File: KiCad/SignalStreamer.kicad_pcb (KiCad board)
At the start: 2 copper layers, 100.3 x 59.1 mm, 48 parts, among them J105 Conn_01x02, T101 Coupled_Inductors_2

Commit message: Ver X1.0
Copied latest changes from backup project
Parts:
- added REF**: MountingHole_2.5mm, MountingHole:MountingHole_2.5mm, F.Cu at (75.2, 86.3)
- added REF**: MountingHole_2.5mm, MountingHole:MountingHole_2.5mm, F.Cu at (96.1, 71.0)
- added REF**: MountingHole_2.5mm, MountingHole:MountingHole_2.5mm, F.Cu at (87.6, 75.4)
- added REF**: MountingHole_2.5mm, MountingHole:MountingHole_2.5mm, F.Cu at (69.9, 63.5)
- added REF**: MountingHole_2.5mm, MountingHole:MountingHole_2.5mm, F.Cu at (74.9, 71.6)
- added REF**: MountingHole_2.5mm, MountingHole:MountingHole_2.5mm, F.Cu at (70.3, 94.6)
- T101: footprint Inductor_THT:Core_150A_2_windings_Horiz_TH -> Inductor_THT:Core_T130_2_windings_Horiz_TH
- moved L101 19.5 mm to (119.0, 63.3), turned to -90 degrees
- moved L101 18.6 mm to (120.6, 63.3), turned to -90 degrees
- moved REF** 12.3 mm to (134.4, 75.5)
- moved REF** 11.4 mm to (134.8, 101.7)
- moved L101 10.9 mm to (102.7, 79.5), turned to -90 degrees
- moved L101 10.8 mm to (101.2, 79.5), turned to -90 degrees
- moved ? 8.33 mm to (123.0, 67.2)
- moved REF** 4.90 mm to (126.7, 63.3)
- moved ? 4.00 mm to (103.9, 106.2)
- moved ? 4.00 mm to (103.9, 112.8)
- moved REF** 4.00 mm to (103.9, 99.7)
- moved ? 3.24 mm to (122.7, 108.3)
- moved T101 3.16 mm to (79.6, 78.9)
- moved REF** 2.91 mm to (126.7, 112.7)
- moved C101 2.83 mm to (97.2, 97.5)
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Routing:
- net Net-(J105-Pin_1): track 13.0 -> 34.3 mm
- net Net-(T101-IN+): track 3.23 -> 7.65 mm
- net Net-(T101-OUT1B): track 8.37 -> 5.29 mm
- net Net-(AE101-A): track 24.8 -> 27.3 mm
- net Net-(D101-K): track 13.7 -> 13.0 mm
- net Net-(D101-A): track 74.0 -> 74.5 mm
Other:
- board text added: "*"
- board text added: "Braid"
- board text added: "Coax"
- board text added: "Counterpoise Elements*"
- board text added: "SignalStreamer Ver 1.0 1 Jan 2026"
- board text added: "Tube"
- board text added: "Vertical"

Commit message: Development
Updates
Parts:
- removed the ? at (118.0, 106.2)
- removed the ? at (118.0, 99.7)
- removed the ? at (118.0, 112.8)
- removed the ? at (103.9, 106.2)
- removed the ? at (103.9, 112.8)
- removed the L101 at (101.2, 79.5)
- removed the L101 at (102.7, 79.5)
- removed the L101 at (119.0, 63.3)
- removed the REF** at (103.9, 99.7)
- added REF**: L_Lipstick_Tube_Variable, Inductor_THT:L_Lipstick_Tube_Variable, F.Cu at (101.2, 79.6)
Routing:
- net Net-(J105-Pin_1): track 34.3 -> 36.2 mm

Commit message: Development
PCB Updates
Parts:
- removed the L101 at (120.6, 63.3)
- L101: renamed from REF**; value L_Lipstick_Tube_Variable -> FB-31-4852
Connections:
- L101 pad 1: (no net) -> Net-(T101-OUT1B)
- L101 pad 2: (no net) -> Net-(J105-Pin_1)
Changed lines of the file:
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@@
 			)
 		)
+		(property "Digi-Key Part No." ""
+			(at 0 0 0)
+			(unlocked yes)
+			(layer "F.Fab")
+			(hide yes)
+			(effects
+				(font
+					(size 1 1)
+					(thickness 0.15)
+				)
+			)
+		)
 		(sheetname "/")
 		(sheetfile "SignalStreamer.kicad_sch")
@@
 			(pinfunction "OUT1A")
 			(pintype "passive")
+			(clearance 0.5)
 			(zone_connect 2)
 		)
@@
 			(pinfunction "OUT1B")
 			(pintype "passive")
+			(clearance 0.5)
 			(zone_connect 2)
 		)
@@
 			)
 		)
-		(property "Datasheet" ""
+		(property "Datasheet" "~"
 			(at 0 0 90)
 			(layer "F.Fab")
@@
 			)
 		)
-		(property "Description" "CONN BNC JACK R/A 50 OHM PCB"
+		(property "Description" "Generic connector, single row, 01x02, script generated (kicad-library-utils/schlib/autogen/connector/)"
 			(at 37.8625 216.6875 0)
 			(layer "F.Fab")
@@
 			)
 		)
-		(property "Link" "https://www.digikey.com/en/products/detail/amphenol-rf/31-5431/80179?utm_adgroup=Coaxial%20Connectors%20%28RF%29&utm_source=google&utm_medium=cpc&utm_campaign=Shopping_Product_Connectors%2C%20Interconnects&utm_term=&utm_content=Coaxial%20Connectors%20%28RF%29&gclid=Cj0KCQjw1rqkBhCTARIsAAHz7K07BKQI4hz-lx2UKWOAkhojF887qRyZwSAGP9HUwnWBejkHZJLi92kaAsMsEALw_wcB"
+		(property "Link" ""
 			(at 37.8625 216.6875 0)
 			(layer "F.Fab")
@@
 			)
 		)
-		(property "Manufacturer" "Amphenol RF"
+		(property "Manufacturer" ""
 			(at 37.8625 216.6875 0)
 			(layer "F.Fab")
@@
 			)
 		)
-		(property "Manufacturer PN" "31-5431"
+		(property "Manufacturer PN" ""
 			(at 37.8625 216.6875 0)
 			(layer "F.Fab")
@@
 			)
 		)
+		(property "Sim.Device" ""
+			(at 0 0 270)
+			(unlocked yes)
+			(layer "F.Fab")
+			(hide yes)
+			(effects
+				(font
+					(size 1 1)
+					(thickness 0.15)
+				)
+			)
+		)
+		(property "Sim.Pins" ""
+			(at 0 0 270)
+			(unlocked yes)
+			(layer "F.Fab")
+			(hide yes)
+			(effects
+				(font
+					(size 1 1)
+					(thickness 0.15)
+				)
+			)
+		)
 		(property ki_fp_filters "Connector*:*_1x??_*")
 		(sheetname "/")
 		(sheetfile "SignalStreamer.kicad_sch")
-		(attr through_hole)
+		(attr through_hole exclude_from_bom)
 		(fp_line
 			(start -7.5 2.3)
@@
 	(footprint ""
 		(layer "F.Cu")
-		(at 120.58 63.31 -90)
-		(property "Reference" "L101"
-			(at 0 0 90)
-			(layer "F.SilkS")
-			(hide yes)
-			(effects
-				(font
-					(size 1.27 1.27)
-					(thickness 0.15)
-				)
-			)
-		)
-		(property "Value" "0.4-1.0uH"
-			(at 0 0 90)
-			(layer "F.Fab")
-			(effects
-				(font
-					(size 1.27 1.27)
-					(thickness 0.15)
-				)
-			)
-		)
-		(property "Datasheet" ""
-			(at 0 0 90)
-			(layer "F.Fab")
-			(hide yes)
-			(effects
-				(font
-					(size 1.27 1.27)
-					(thickness 0.15)
-				)
-			)
-		)
-		(property "Description" ""
-			(at 0 0 90)
-			(layer "F.Fab")
-			(hide yes)
-			(effects
-				(font
-					(size 1.27 1.27)
-					(thickness 0.15)
-				)
-			)
-		)
-		(sheetname "/")
-		(sheetfile "SignalStreamer.kicad_sch")
-		(pad "2" thru_hole circle
-			(at 0 0 270)
-			(size 2.6 2.6)
-			(drill 1.1)
-			(layers "*.Cu" "*.Mask")
-			(remove_unused_layers no)
-			(net 15 "Net-(J105-Pin_1)")
-			(pinfunction "2")
-			(pintype "passive")
-			(clearance 0.5)
-			(zone_connect 2)
-		)
-		(embedded_fonts no)
-	)
-	(footprint ""
-		(layer "F.Cu")
 		(at 122.97 67.19)
 		(property "Reference" ""
@@
 		(descr "Inductor, Axial series, Axial, Horizontal, pin pitch=10.16mm, length*diameter=6.6*2.7mm^2, Vishay, IM-2, http://www.vishay.com/docs/34030/im.pdf")
 		(tags "Inductor Axial series Axial Horizontal pin pitch 10.16mm  length 6.6mm diameter 2.7mm Vishay IM-2")
-		(property "Reference" "REF**"
+		(property "Reference" "L101"
 			(at 5.08 -2.47 0)
 			(layer "F.SilkS")
+			(hide yes)
 			(effects
 				(font
@@
 			)
 		)
-		(property "Value" "L_Lipstick_Tube_Variable"
+		(property "Value" "FB-31-4852"
 			(at 5.08 2.47 0)
 			(layer "F.Fab")
+			(hide yes)
 			(effects
 				(font
@@
 			)
 		)
-		(property "Description" ""
+		(property "Description" "Lipstick tube variable inductor"
 			(at 0 0 0)
 			(layer "F.Fab")
@@
 			)
 		)
+		(property "Digi-Key Part No." ""
+			(at 0 0 0)
+			(unlocked yes)
+			(layer "F.Fab")
+			(hide yes)
+			(effects
+				(font
+					(size 1 1)
+					(thickness 0.15)
+				)
+			)
+		)
+		(property "Link" ""
+			(at 0 0 0)
+			(unlocked yes)
+			(layer "F.Fab")
+			(hide yes)
+			(effects
+				(font
+					(size 1 1)
+					(thickness 0.15)
+				)
+			)
+		)
+		(property "Manufacturer" "Amidon"
+			(at 0 0 0)
+			(unlocked yes)
+			(layer "F.Fab")
+			(hide yes)
+			(effects
+				(font
+					(size 1 1)
+					(thickness 0.15)
+				)
+			)
+		)
+		(property "Manufacturer PN" "FB-31-4852"
+			(at 0 0 0)
+			(unlocked yes)
+			(layer "F.Fab")
+			(hide yes)
+			(effects
+				(font
+					(size 1 1)
+					(thickness 0.15)
+				)
+			)
+		)
+		(sheetname "/")
+		(sheetfile "SignalStreamer.kicad_sch")
 		(attr through_hole)
 		(fp_line
-			(start 1.04 0)
-			(end 1.66 0)
+			(start 1.73 -20.3)
+			(end 1.73 -9.53)
 			(stroke
-				(width 0.12)
+				(width 0.25)
 				(type solid)
 			)
@@
 		)
 		(fp_line
-			(start 1.73 35.92)
-			(end 1.73 -20.3)
+			(start 1.73 -5.75)
+			(end 1.73 18.5)
+			(stroke
+				(width 0.25)
+				(type solid)
+			)
+			(layer "F.SilkS")
+		)
+		(fp_line
+			(start 1.73 21.64)
+			(end 1.73 25.06)
+			(stroke
+				(width 0.25)
+				(type solid)
+			)
+			(layer "F.SilkS")
+		)
+		(fp_line
+			(start 1.73 28.24)
+			(end 1.73 31.63)
 			(stroke
 				(width 0.25)
@@
 		)
 		(fp_line
-			(start 17.81 -20.3)
-			(end 17.81 35.92)
+			(start 17.84 -20.375)
+			(end 17.84 -9.605)
+			(stroke
+				(width 0.25)
+				(type solid)
+			)
+			(layer "F.SilkS")
+		)
+		(fp_line
+			(start 17.84 -5.825)
+			(end 17.84 18.5)
+			(stroke
+				(width 0.25)
+				(type solid)
+			)
+			(layer "F.SilkS")
+		)
+		(fp_line
+			(start 17.84 21.565)
+			(end 17.84 24.985)
+			(stroke
+				(width 0.25)
+				(type solid)
+			)
+			(layer "F.SilkS")
+		)
+		(fp_line
+			(start 17.84 28.165)
+			(end 17.84 31.555)
 			(stroke
 				(width 0.25)
@@
 			(layers "*.Cu" "*.Mask")
 			(remove_unused_layers no)
+			(net 9 "Net-(T101-OUT1B)")
+			(pinfunction "1")
+			(pintype "passive")
 			(clearance 0.5)
 			(zone_connect 2)
@@
 			(size 1.524 5)
 			(layers "B.Cu" "B.Mask" "B.Paste")
+			(net 9 "Net-(T101-OUT1B)")
+			(pinfunction "1")
+			(pintype "passive")
 			(zone_connect 2)
 		)
@@
 			(size 1.524 5)
 			(layers "B.Cu" "B.Mask" "B.Paste")
+			(net 15 "Net-(J105-Pin_1)")
+			(pinfunction "2")
+			(pintype "passive")
 			(clearance 0.5)
 			(zone_connect 2)
@@
 			(layers "*.Cu" "*.Mask")
 			(remove_unused_layers no)
+			(net 15 "Net-(J105-Pin_1)")
+			(pinfunction "2")
+			(pintype "passive")
 			(clearance 0.5)
 			(zone_connect 2)
@@
 			)
 		)
-		(property "Datasheet" ""
+		(property "Datasheet" "https://www.st.com/content/ccc/resource/technical/document/datasheet/a8/9d/10/57/ac/a3/4f/81/CD00000759.pdf/files/CD00000759.pdf/jcr:content/translations/en.CD00000759.pdf"
 			(at 0 0 0)
 			(layer "F.Fab")
@@
 			)
 		)
-		(property "Description" ""
+		(property "Description" "RF DIODE SCHOTTKY 70V 430MW DO35"
 			(at 0 0 0)
 			(layer "F.Fab")
@@
 			)
 		)
-		(property "Datasheet" ""
+		(property "Datasheet" "https://www.st.com/content/ccc/resource/technical/document/datasheet/a8/9d/10/57/ac/a3/4f/81/CD00000759.pdf/files/CD00000759.pdf/jcr:content/translations/en.CD00000759.pdf"
 			(at 0 0 180)
 			(layer "F.Fab")
@@
 			)
 		)
-		(property "Description" ""
+		(property "Description" "RF DIODE SCHOTTKY 70V 430MW DO35"
 			(at 0 0 180)
 			(layer "F.Fab")
@@
 	)
 	(zone
-		(net 0)
-		(net_name "")
-		(layer "F.Cu")
-		(hatch edge 0.5)
-		(connect_pads
-			(clearance 0)
-		)
-		(min_thickness 0.25)
-		(filled_areas_thickness no)
-		(keepout
-			(tracks not_allowed)
-			(vias not_allowed)
-			(pads not_allowed)
-			(copperpour allowed)
-			(footprints allowed)
-		)
-		(placement
-			(enabled no)
-			(sheetname "")
-		)
-		(fill
-			(thermal_gap 0.5)
-			(thermal_bridge_width 0.5)
-		)
-		(polygon
-			(pts
-				(xy 103.15 63.5) (xy 118.54 63.52) (xy 118.54 80.29) (xy 102.76 80.1) (xy 102.95 63.33)
-			)
-		)
-	)
-	(zone
 		(net 4)
 		(net_name "GND")
@@
 			(tracks not_allowed)
 			(vias not_allowed)
-			(pads not_allowed)
+			(pads allowed)
 			(copperpour not_allowed)
 			(footprints allowed)

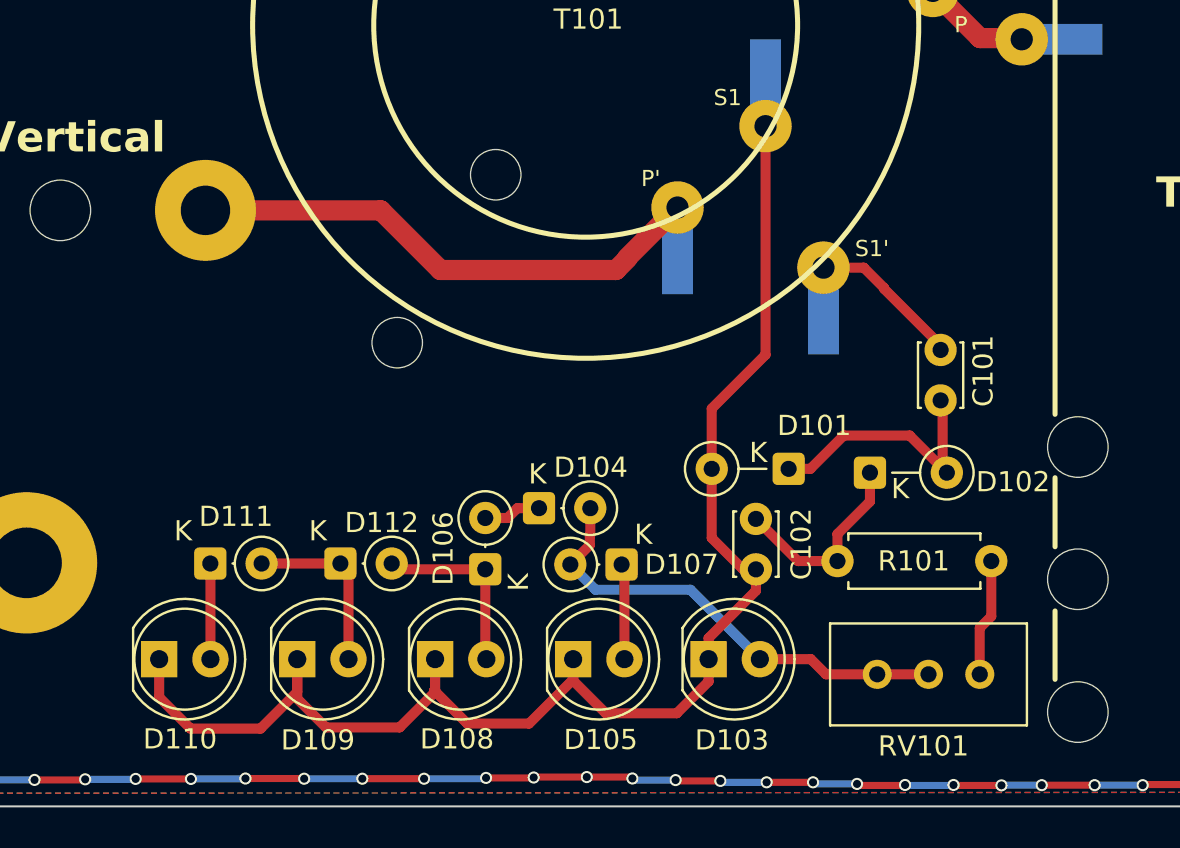
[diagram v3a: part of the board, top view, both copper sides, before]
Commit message: Ver 1.0
Redesign of LED tuning indicator. All gerbers updated.
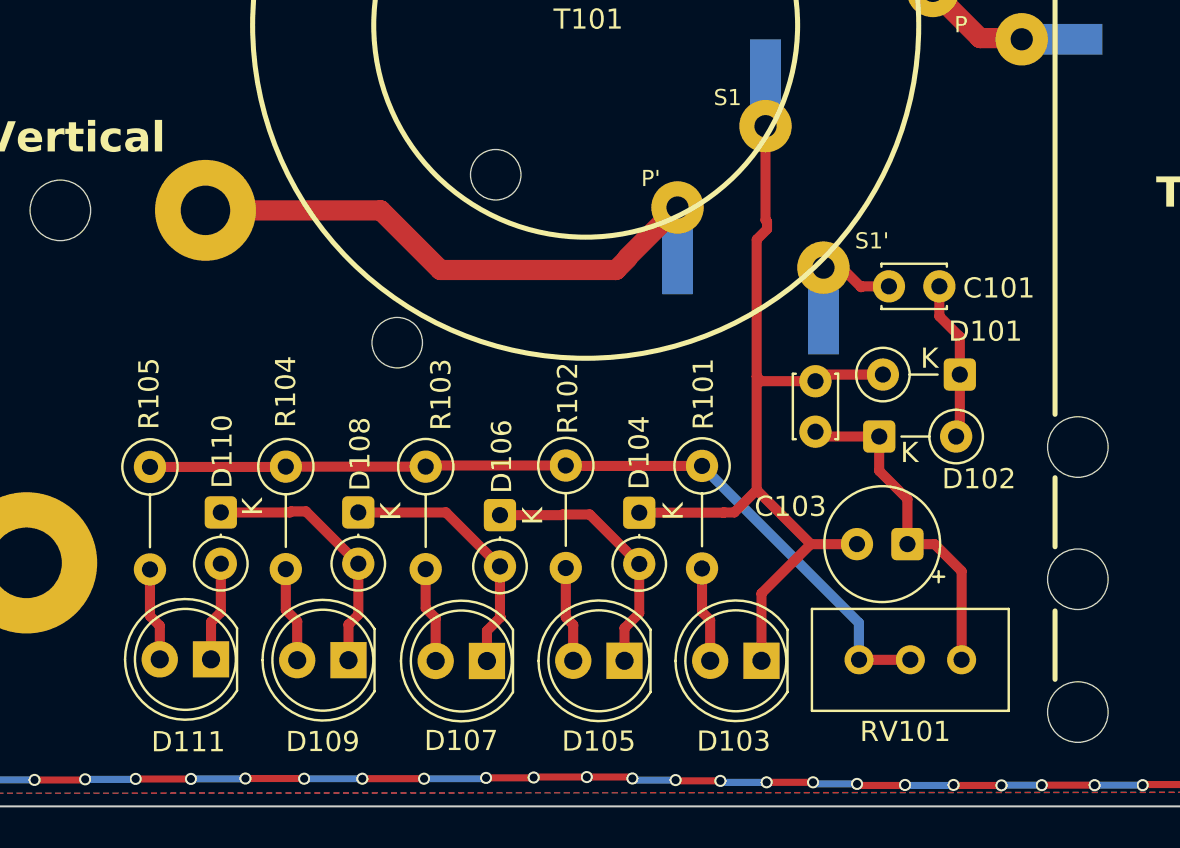
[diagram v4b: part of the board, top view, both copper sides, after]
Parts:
- removed the D105 at (81.4, 105.6)
- removed the D111 at (61.0, 105.5)
- removed D112: 1N4148, Diode_THT:D_DO-35_SOD27_P2.54mm_Vertical_KathodeUp
- added C103: 10uF, Capacitor_THT:CP_Radial_Tantal_D5.5mm_P2.50mm, F.Cu at (95.6, 104.6)
- added D108: 1N4148, Diode_THT:D_DO-35_SOD27_P2.54mm_Vertical_KathodeUp, F.Cu at (68.4, 103.0)
- added D110: 1N4148, Diode_THT:D_DO-35_SOD27_P2.54mm_Vertical_KathodeUp, F.Cu at (61.5, 103.0)
- added R102: 470, Resistor_THT:R_Axial_DIN0207_L6.3mm_D2.5mm_P5.08mm_Vertical, F.Cu at (78.6, 100.7)
- added R103: 470, Resistor_THT:R_Axial_DIN0207_L6.3mm_D2.5mm_P5.08mm_Vertical, F.Cu at (71.7, 100.7)
- added R104: 470, Resistor_THT:R_Axial_DIN0207_L6.3mm_D2.5mm_P5.08mm_Vertical, F.Cu at (64.8, 100.7)
- added R105: 470, Resistor_THT:R_Axial_DIN0207_L6.3mm_D2.5mm_P5.08mm_Vertical, F.Cu at (58.0, 100.7)
- C101, C102: value 470 nF -> 470nF
- R101: footprint Resistor_THT:R_Axial_DIN0207_L6.3mm_D2.5mm_P7.62mm_Horizontal -> Resistor_THT:R_Axial_DIN0207_L6.3mm_D2.5mm_P5.08mm_Vertical
- RV101: value 10k -> 2k
- moved D101 9.68 mm to (98.2, 96.2)
- moved R101 8.20 mm to (85.4, 100.7), turned to -90 degrees
- moved C101 5.65 mm to (97.2, 91.8), turned to 180 degrees
- moved C102 5.23 mm to (91.0, 99.0), turned to 90 degrees
- moved D104 4.97 mm to (82.3, 103.0), turned to -90 degrees
- moved D106 2.78 mm to (75.4, 103.1), turned to -90 degrees
- moved D103 2.62 mm to (88.3, 110.3), turned to 180 degrees
- moved D107 2.57 mm to (74.7, 110.4), turned to 180 degrees
- moved D111 2.57 mm to (61.1, 110.3), turned to 180 degrees
- moved D105 2.55 mm to (81.5, 110.3), turned to 180 degrees
- moved D109 2.54 mm to (67.9, 110.3), turned to 180 degrees
- moved D102 1.85 mm to (94.2, 99.2)
- moved RV101 1.15 mm to (98.2, 110.3)
- renumbered D107 to D105, D108 to D107, D110 to D111
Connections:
- D104 pad 1: Net-(D104-K) -> Net-(D101-A)
- D104 pad 2: Net-(D103-A) -> Net-(D104-A)
- D105 pad 1: Net-(D101-A) -> Net-(D104-A)
- D106 pad 1: Net-(D106-K) -> Net-(D104-A)
- D106 pad 2: Net-(D104-K) -> Net-(D106-A)
- D107 pad 1: Net-(D101-A) -> Net-(D106-A)
- D107 pad 2: Net-(D106-K) -> Net-(D107-A)
- D109 pad 1: Net-(D101-A) -> Net-(D108-A)
- D111 pad 1: Net-(D101-A) -> Net-(D110-A)
- R101 pad 1: Net-(D102-K) -> Net-(R101-Pad1)
- R101 pad 2: Net-(R101-Pad2) -> Net-(D103-A)
- RV101 pad 1: Net-(R101-Pad2) -> Net-(D102-K)
- RV101 pad 2: Net-(D103-A) -> Net-(R101-Pad1)
- RV101 pad 3: Net-(D103-A) -> Net-(R101-Pad1)
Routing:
- net Net-(R101-Pad1): track 0.00 -> 42.9 mm
- net Net-(D101-A): track 74.5 -> 43.9 mm
- net Net-(D103-A): track 23.2 -> 4.74 mm
- net Net-(D106-A): track 0.00 -> 13.1 mm
- net Net-(D104-A): track 0.00 -> 13.0 mm
- net Net-(D108-A): track 0.00 -> 12.9 mm
- net Net-(D106-K): track 9.23 -> 0.00 mm
- net Net-(D102-K): track 9.95 -> 16.6 mm
- net Net-(R101-Pad2): track 5.85 -> 0.00 mm
- net Net-(D101-K): track 13.0 -> 7.93 mm
- net Net-(D110-A): track 0.00 -> 4.95 mm
- net Net-(D107-A): track 0.00 -> 4.76 mm
- net Net-(D109-A): track 8.81 -> 4.74 mm
- net Net-(T101-IN+): track 7.65 -> 3.66 mm
- net Net-(D104-K): track 2.87 -> 0.00 mm

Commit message: PCB Updates
Corrects a problem with horizontal radials connection to coax ground
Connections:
- REF** pad : (no net) -> GND (x4)
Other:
- board text added: "D103"
- board text added: "D105"
- board text added: "D107"
- board text added: "D109"
- board text added: "D111"
